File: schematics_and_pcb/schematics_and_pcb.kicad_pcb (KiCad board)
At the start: 2 copper layers, 44.5 x 90 mm, 61 parts, among them J1 RND 205-00623, J2 RND 205-00627, J3 Motor con, Q1 PMV213SN, SW1 RND 210-00210, U1 MIC5235YM5-TR, U2 AP2125N-3.3TRG1, U3 PWM3389DM-T3QU, U4 STM32F411RETx, Y1 YLFXTAL029370

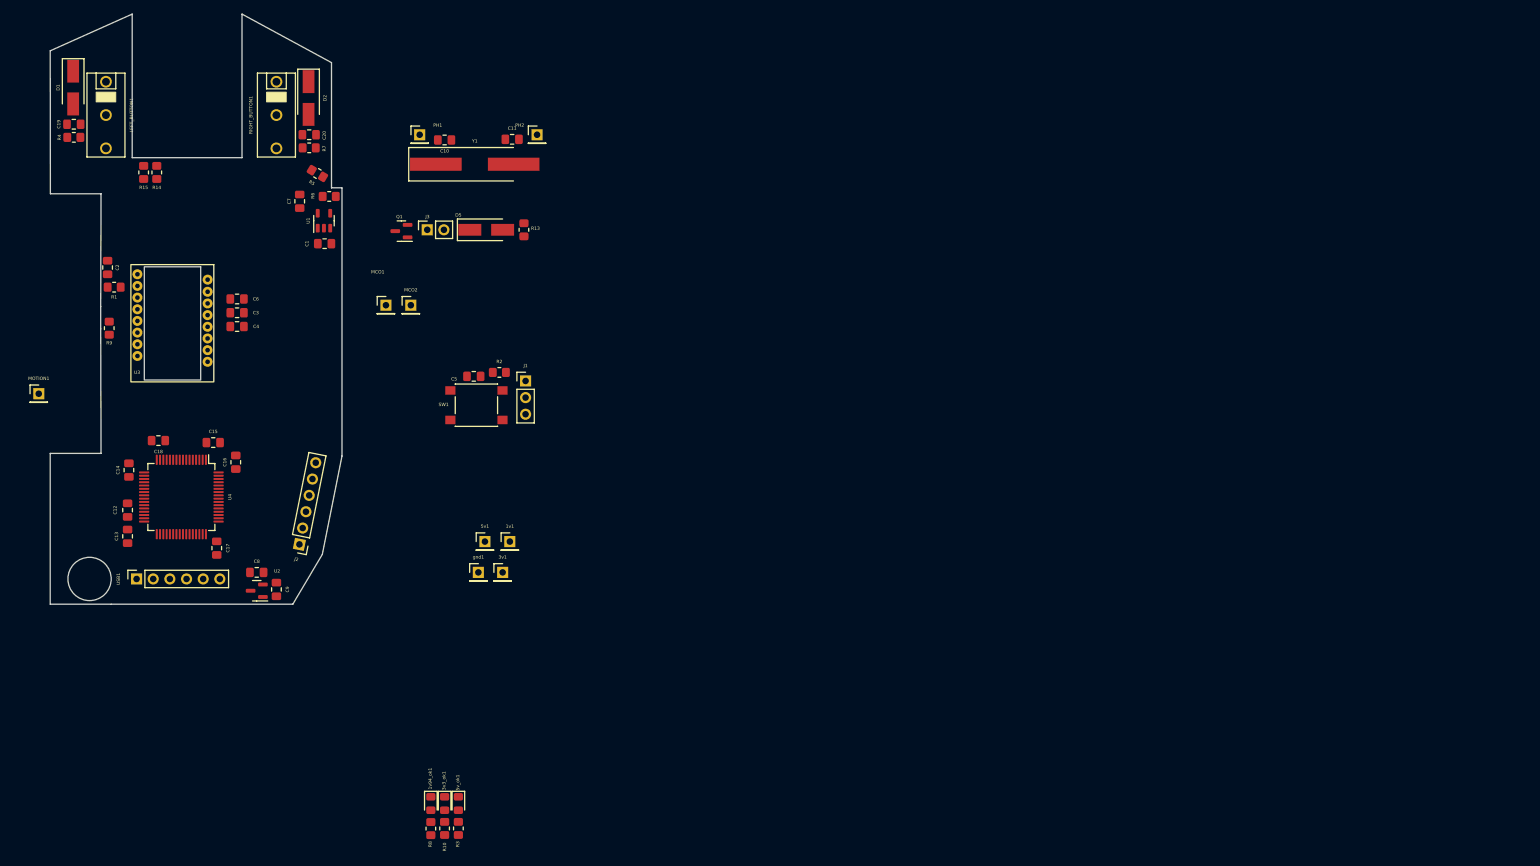
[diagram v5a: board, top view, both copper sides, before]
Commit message: added mounting holes
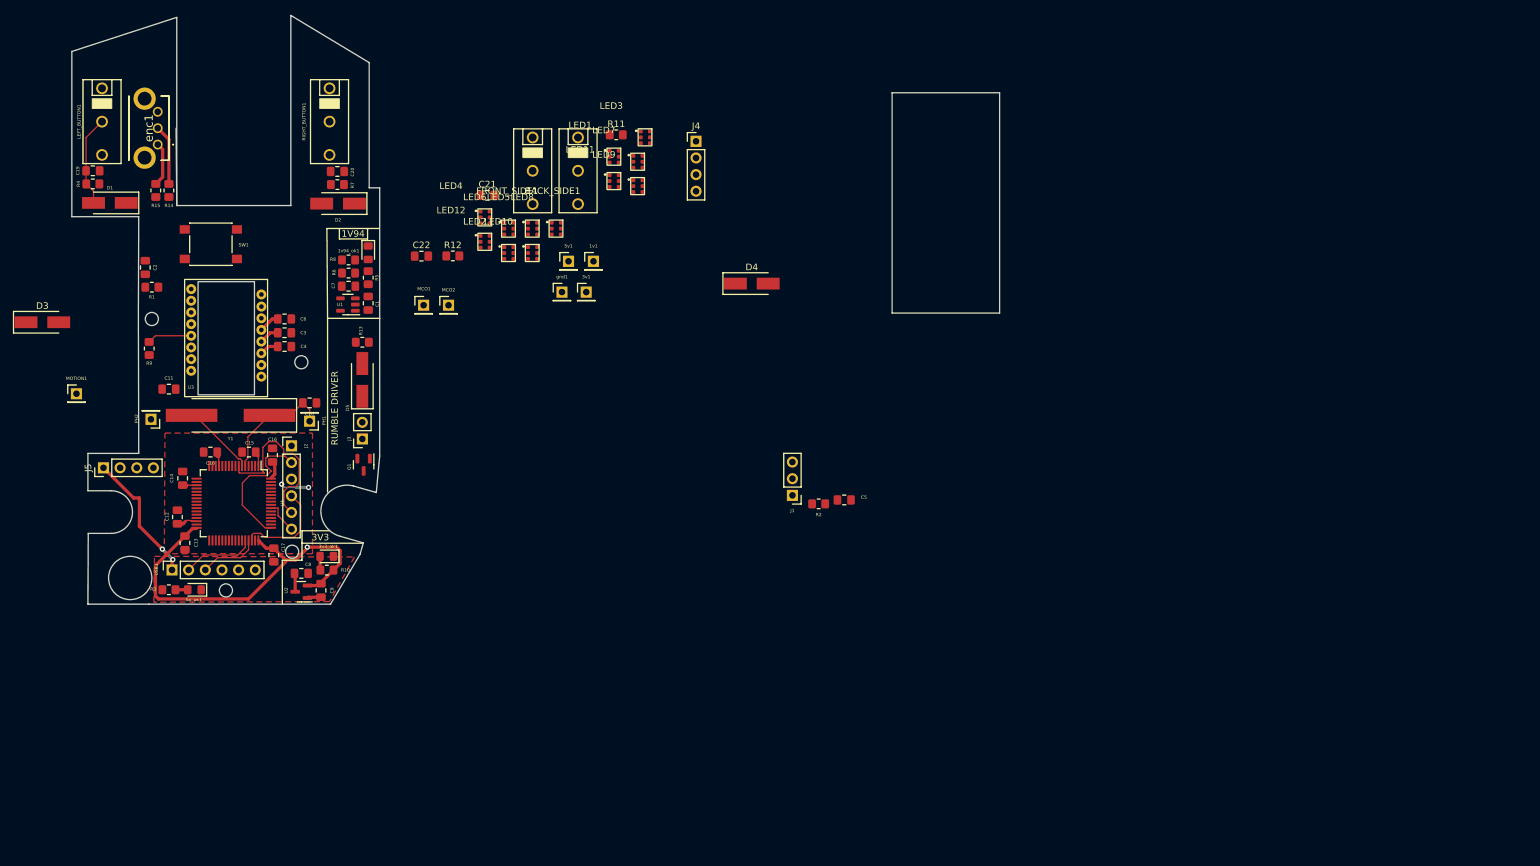
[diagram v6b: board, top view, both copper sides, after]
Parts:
- added BACK_SIDE1: D2F-01F, mouse:D2F-01F, F.Cu at (97.0, 38.0)
- added C21: 10u, Capacitor_SMD:C_0805_2012Metric_Pad1.18x1.45mm_HandSolder, F.Cu at (83.2, 41.7)
- added C22: 10u, Capacitor_SMD:C_0805_2012Metric_Pad1.18x1.45mm_HandSolder, F.Cu at (73.1, 51.0)
- added D3: S1A, Diode_SMD:D_SMA_Handsoldering, F.Cu at (15.3, 61.1)
- added D4: S1A, Diode_SMD:D_SMA_Handsoldering, F.Cu at (123.5, 55.2)
- added FRONT_SIDE1: D2F-01F, mouse:D2F-01F, F.Cu at (90.1, 38.0)
- added J4: Conn_01x04_Male, Connector_PinHeader_2.54mm:PinHeader_1x04_P2.54mm_Vertical, F.Cu at (115.0, 33.5)
- added J5: Conn_01x04_Male, Connector_PinHeader_2.54mm:PinHeader_1x04_P2.54mm_Vertical, F.Cu at (24.6, 83.3)
- added LED1: RND_135-00249, mouse:RND_135-00249, F.Cu at (102.5, 35.8)
- added LED10: RND_135-00249, mouse:RND_135-00249, F.Cu at (90.1, 50.5)
- added LED11: RND_135-00249, mouse:RND_135-00249, F.Cu at (102.5, 39.6)
- added LED12: RND_135-00249, mouse:RND_135-00249, F.Cu at (82.8, 48.8)
- added LED2: RND_135-00249, mouse:RND_135-00249, F.Cu at (86.4, 50.5)
- added LED3: RND_135-00249, mouse:RND_135-00249, F.Cu at (107.3, 32.9)
- added LED4: RND_135-00249, mouse:RND_135-00249, F.Cu at (82.8, 45.1)
- added LED5: RND_135-00249, mouse:RND_135-00249, F.Cu at (90.1, 46.8)
- added LED6: RND_135-00249, mouse:RND_135-00249, F.Cu at (86.4, 46.8)
- added LED7: RND_135-00249, mouse:RND_135-00249, F.Cu at (106.1, 36.6)
- added LED8: RND_135-00249, mouse:RND_135-00249, F.Cu at (93.7, 46.8)
- added LED9: RND_135-00249, mouse:RND_135-00249, F.Cu at (106.1, 40.3)
- added R11: 4.7k, Resistor_SMD:R_0805_2012Metric_Pad1.20x1.40mm_HandSolder, F.Cu at (102.8, 32.5)
- added R12: 4.7k, Resistor_SMD:R_0805_2012Metric_Pad1.20x1.40mm_HandSolder, F.Cu at (77.9, 51.0)
- added enc1: EC10E1220505, mouse:EC10E1220505, F.Cu at (32.9, 34.0)
- moved R8 87.6 mm to (62.0, 51.6), turned to 0 degrees
- moved 1v94_ok1 84.5 mm to (65.0, 50.5)
- moved PH2 73.2 mm to (31.9, 75.9), turned to 180 degrees
- moved C11 64.7 mm to (34.6, 71.3)
- moved C5 59.6 mm to (137.6, 88.2), turned to 180 degrees
- moved R3 57.2 mm to (34.6, 101.9), turned to 0 degrees
- moved Y1 53.4 mm to (44.0, 75.3), turned to 180 degrees
- moved R2 52.7 mm to (133.7, 88.8), turned to 180 degrees
- moved 5v_ok1 51.8 mm to (38.5, 101.9), turned to 180 degrees
- moved SW1 47.4 mm to (41.0, 49.2), turned to 180 degrees
- moved PH1 46.8 mm to (56.1, 76.2), turned to 180 degrees
- moved C10 45.1 mm to (56.1, 73.4)
- moved 1v1 44.6 mm to (99.3, 51.8)
- moved 3v1 44.6 mm to (98.2, 56.5)
- moved 5v1 44.6 mm to (95.5, 51.8)
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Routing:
- net VDDIO: track 0.00 -> 76.3 mm, vias 0 -> 3
- net NRST: track 0.00 -> 26.5 mm
- net +5V: track 0.00 -> 23.4 mm, vias 0 -> 2
- net SWDCLK: track 0.00 -> 21.1 mm
- net PH0: track 0.00 -> 18.4 mm
- net SWDIO: track 0.00 -> 14.9 mm
- net PH1: track 0.00 -> 14.2 mm
- net LEFT_STATE: track 0.00 -> 13.9 mm
- net D-: track 0.00 -> 11.1 mm
- net D+: track 0.00 -> 9.29 mm
- net PHASE_A: track 0.00 -> 9.20 mm
- net SPI2_MISO: track 0.00 -> 6.79 mm
- net PHASE_B: track 0.00 -> 6.75 mm
- net SWO: track 0.00 -> 5.11 mm
- net Net-(C12-Pad1): track 0.00 -> 3.19 mm
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- added copper zone on F.Cu, net +5V
- added copper zone on F.Cu, net VDDIO
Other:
- board size 44.5 x 90 mm -> 141.5 x 89.8 mm
- board text added: "1V94"
- board text added: "3V3"
- board text added: "RUMBLE DRIVER"

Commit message: added routes for all signals except buttons and scrollwheel
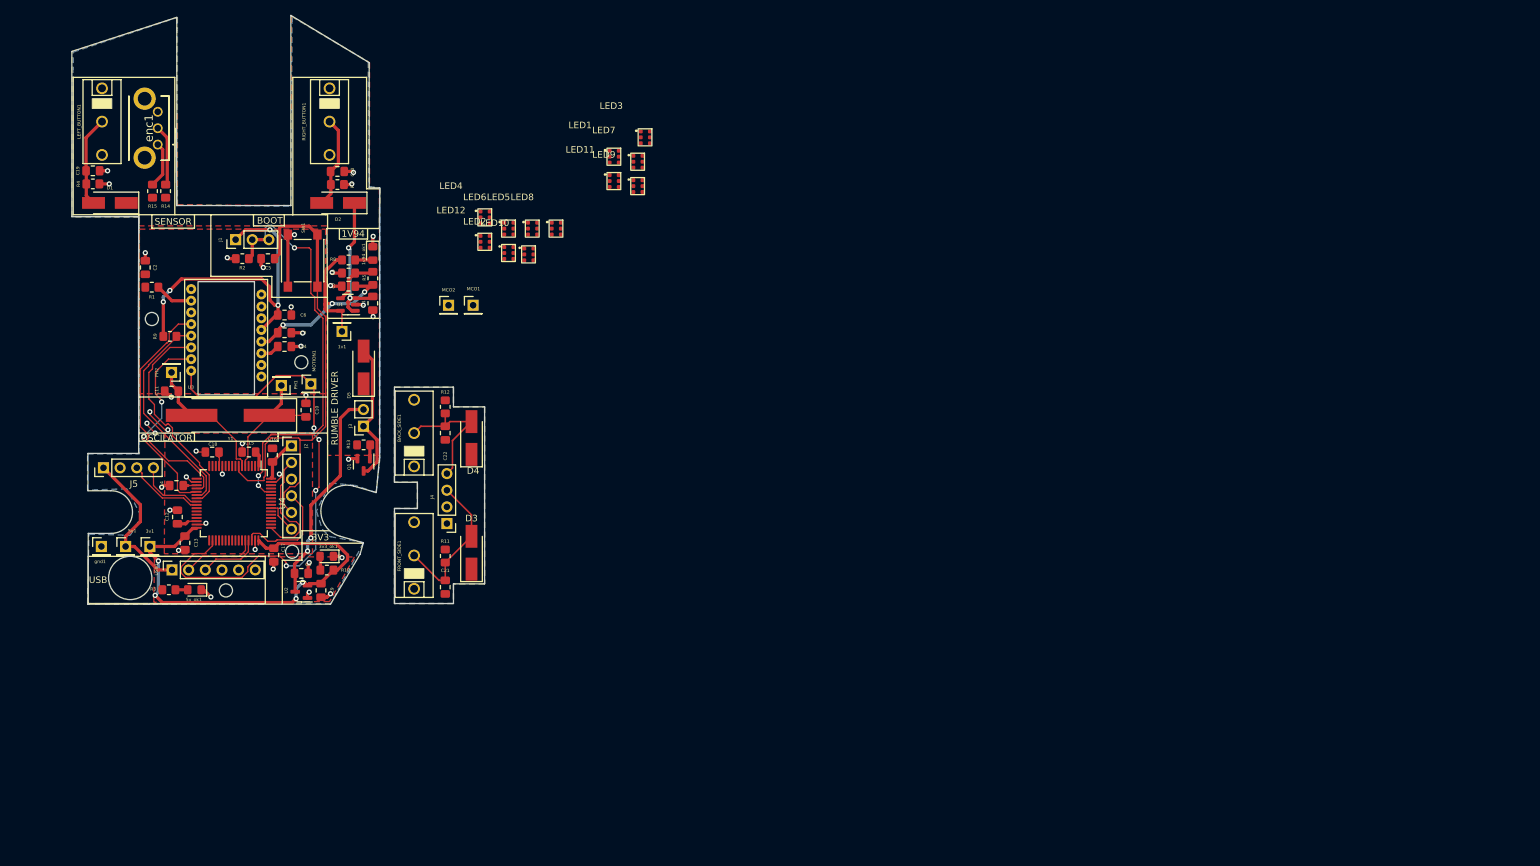
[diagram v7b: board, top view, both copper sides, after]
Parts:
- U4: value STM32F411RETx -> STM32F401RBTx
- moved R2 95.5 mm to (45.8, 51.4)
- moved C5 95.3 mm to (49.7, 51.4), turned to 0 degrees
- moved J1 93.5 mm to (44.8, 48.5), turned to 90 degrees
- moved 5v1 80.3 mm to (28.0, 95.3)
- moved gnd1 80.3 mm to (24.3, 95.3)
- moved 3v1 77.0 mm to (31.7, 95.3)
- moved D3 74.3 mm to (80.8, 96.2), turned to 90 degrees
- moved J4 69.6 mm to (77.0, 91.8), turned to 180 degrees
- moved R11 69.3 mm to (76.8, 96.8), turned to -90 degrees
- moved FRONT_SIDE1 61.4 mm to (72.0, 96.7), turned to 180 degrees
- moved C21 60.1 mm to (76.8, 101.5), turned to 90 degrees
- moved D4 48.8 mm to (80.8, 78.8), turned to 90 degrees
- moved BACK_SIDE1 47.2 mm to (72.0, 78.0), turned to 180 degrees
- moved 1v1 39.8 mm to (61.0, 62.5), turned to 180 degrees
- moved MOTION1 35.8 mm to (56.2, 70.5)
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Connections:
- C18 pad 1: VDDIO -> Net-(C18-Pad1)
- U4 pad 10: SPI2_MISO -> unconnected-(U4-Pad10)
- U4 pad 11: SPI2_MOSI -> unconnected-(U4-Pad11)
- U4 pad 13: VDDIO -> Net-(C18-Pad1)
- U4 pad 2: RUMBLE -> unconnected-(U4-Pad2)
- U4 pad 20: unconnected-(U4-Pad20) -> SPI2_NCS
- U4 pad 21: unconnected-(U4-Pad21) -> SPI2_SCK
- U4 pad 22: unconnected-(U4-Pad22) -> SPI2_MISO
- U4 pad 23: unconnected-(U4-Pad23) -> SPI2_MOSI
- U4 pad 24: unconnected-(U4-Pad24) -> BACK_STATE
- U4 pad 25: unconnected-(U4-Pad25) -> FRONT_STATE
- U4 pad 29: SPI2_SCK -> unconnected-(U4-Pad29)
- U4 pad 33: SPI2_NCS -> unconnected-(U4-Pad33)
- U4 pad 56: LEFT_STATE -> unconnected-(U4-Pad56)
- U4 pad 57: RIGHT_STATE -> unconnected-(U4-Pad57)
- U4 pad 58: FRONT_STATE -> unconnected-(U4-Pad58)
- U4 pad 59: BACK_STATE -> unconnected-(U4-Pad59)
- U4 pad 61: PHASE_A -> unconnected-(U4-Pad61)
- U4 pad 62: PHASE_B -> unconnected-(U4-Pad62)
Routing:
- net MOTION: track 0.00 -> 81.8 mm, vias 0 -> 4
- net BOOT0: track 0.00 -> 63.3 mm, vias 0 -> 3
- net GND: track 2.11 -> 63.9 mm, vias 0 -> 39
- net +5V: track 23.4 -> 78.5 mm, vias 2 -> 4
- net VDDIO: track 76.3 -> 127.5 mm, vias 3 -> 8
- net NRST: track 26.5 -> 75.8 mm
- net VDD: track 3.06 -> 39.5 mm, vias 0 -> 3
- net SPI2_NCS: track 0.00 -> 36.2 mm
- net FRONT_STATE: track 0.00 -> 35.2 mm
- net SPI2_MOSI: track 0.00 -> 33.3 mm
- net BACK_STATE: track 0.00 -> 31.2 mm
- net SPI2_SCK: track 0.00 -> 31.1 mm, vias 0 -> 2
- net SPI2_MISO: track 6.79 -> 33.6 mm
- net Net-(D5-Pad2): track 0.00 -> 21.5 mm
- net RIGHT_STATE: track 0.00 -> 14.0 mm
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- added copper zone on B.Cu, net GND
- added copper zone on F.Cu, net VDD
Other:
- board size 141.5 x 89.8 mm -> 63 x 89.8 mm
- board text added: "BOOT"
- board text added: "EPICLY PRO GAMER MOUSE"
- board text added: "MAIN MOUSE BOARD"
- board text added: "OSCILATOR"
- board text added: "SENSOR"
- board text added: "SIDE BUTTONS"
- board text added: "USB"

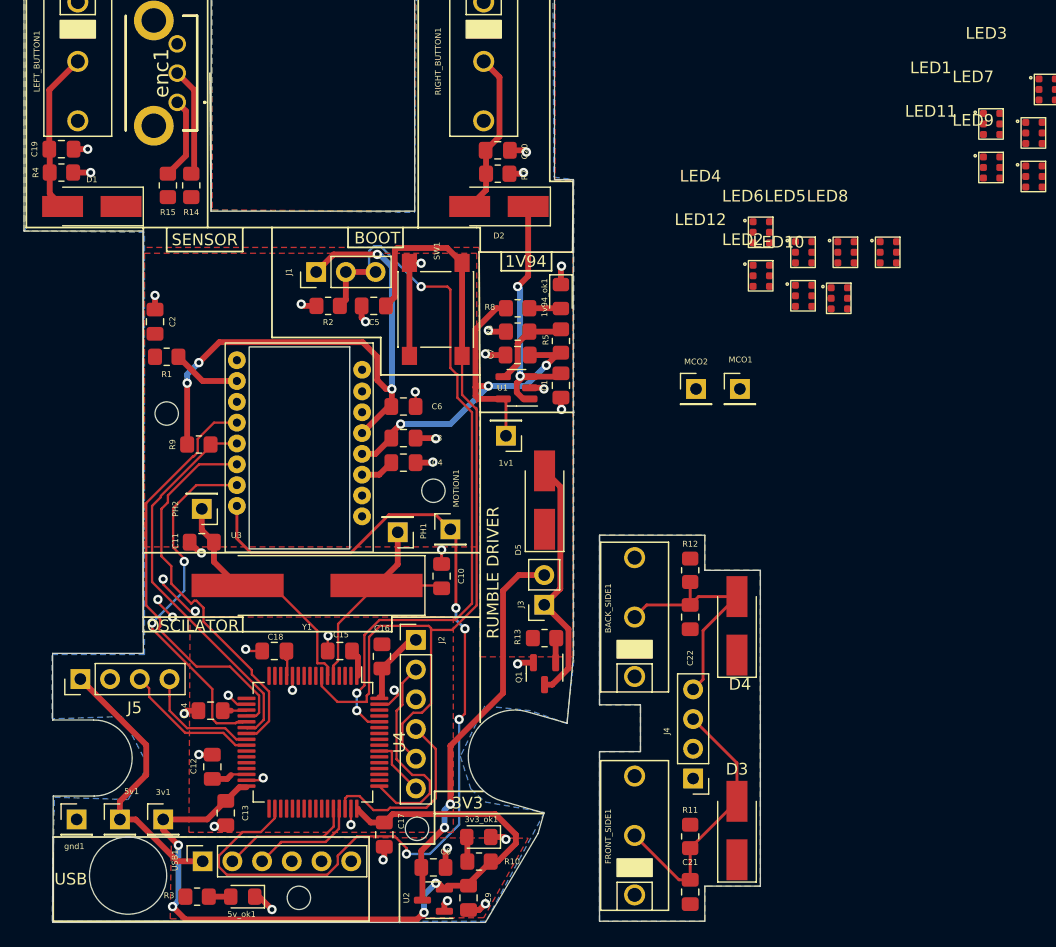
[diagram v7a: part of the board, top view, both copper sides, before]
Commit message: added routes for all buttons
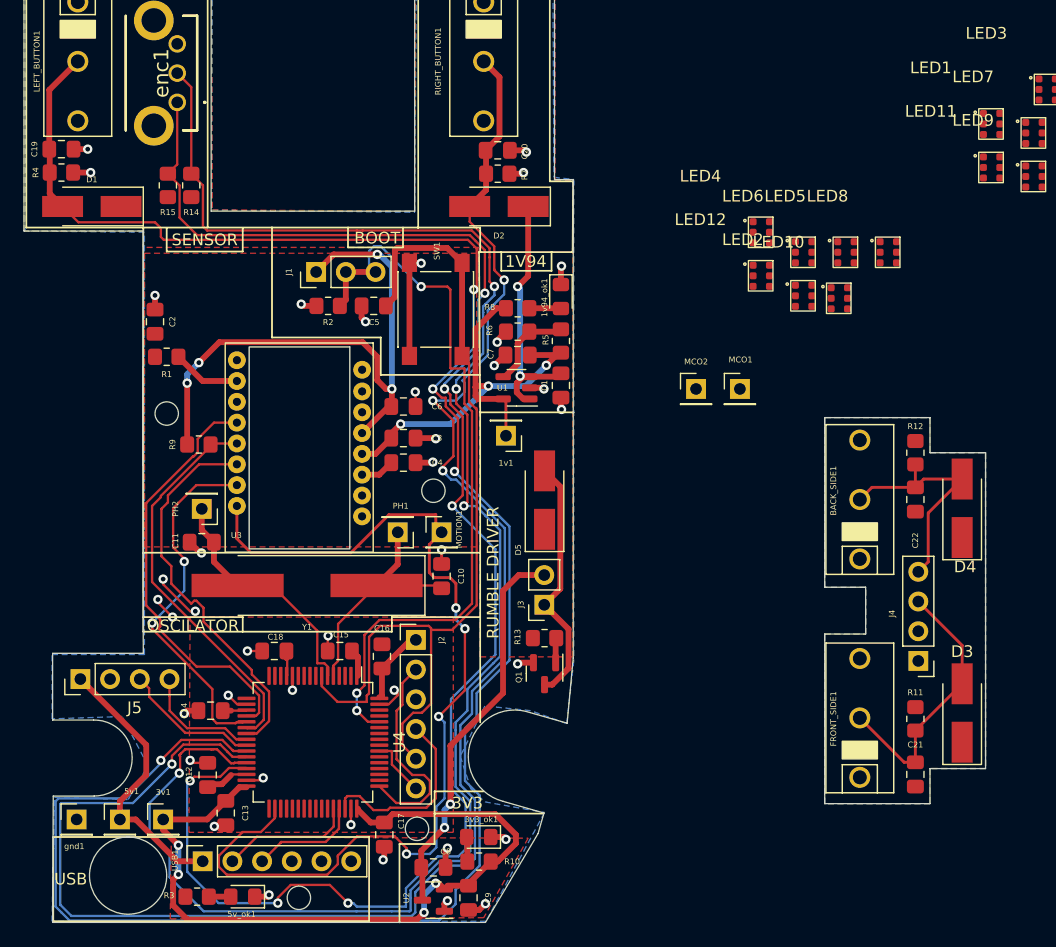
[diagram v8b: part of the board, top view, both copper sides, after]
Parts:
- moved BACK_SIDE1 21.7 mm to (91.2, 68.0)
- moved C21 21.7 mm to (96.0, 91.5)
- moved C22 21.7 mm to (96.0, 68.0)
- moved D3 21.7 mm to (100.0, 86.2)
- moved D4 21.7 mm to (100.0, 68.7)
- moved FRONT_SIDE1 21.7 mm to (91.2, 86.6)
- moved J4 21.7 mm to (96.2, 81.8)
- moved R11 21.7 mm to (96.0, 86.7)
- moved R12 21.7 mm to (96.0, 64.0)
- moved C12 0.81 mm to (35.5, 91.5)
- moved MOTION1 0.79 mm to (55.5, 70.8)
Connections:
- U4 pad 26: unconnected-(U4-Pad26) -> LEFT_STATE
- U4 pad 27: unconnected-(U4-Pad27) -> RIGHT_STATE
- U4 pad 28: unconnected-(U4-Pad28) -> PHASE_A
- U4 pad 29: unconnected-(U4-Pad29) -> PHASE_B
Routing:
- net LEFT_STATE: track 13.9 -> 178.5 mm, vias 0 -> 4
- net PHASE_A: track 9.30 -> 146.4 mm, vias 0 -> 4
- net RIGHT_STATE: track 14.0 -> 146.9 mm, vias 0 -> 4
- net PHASE_B: track 7.05 -> 137.8 mm, vias 0 -> 6
- net MOTION: track 81.8 -> 83.9 mm
- net GND: track 63.9 -> 62.7 mm
- net Net-(C12-Pad1): track 3.09 -> 3.78 mm
- net BOOT0: track 63.3 -> 64.0 mm
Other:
- board size 63 x 89.8 mm -> 82.2 x 89.8 mm
- board text added: "BRIDGING THE GAP IN GND"
